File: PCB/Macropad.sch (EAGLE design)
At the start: 74 parts, among them IC1 LM2937, U1 EC11E09244AQ, X1 ZX62D-B-5PA8

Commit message: Added Matthew's urgent updates
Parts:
- added C13: 0.1uf, EE445L:CAPACITOR025-024X044
- added JP1: (no value), EE445L:PINHD-1X4
- added U2: TPD2E001DRLR, TPD2E001DRLR:TPD2E001DRLR
- C1: value 0.01uf -> 10uF
- C2, C4: value 0.1uf -> 0.1uF
- C3, C5: value 0.01uf -> 0.1uF
- C9: value 0.1uf -> 1.0uf
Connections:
- net +5V: now also C13.1, JP1.1, U2.VCC
- net D+: now also JP1.2, U2.IO1
- net D-: now also JP1.3, U2.IO2
- net GND: now also C13.2, JP1.4, U2.GND
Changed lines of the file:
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@@
 </classes>
 <parts>
-<part name="C1" library="EE445L" deviceset="CAPACITOR" device="025-024X044" value="0.01uf"/>
-<part name="C2" library="EE445L" deviceset="CAPACITOR" device="025-024X044" value="0.1uf"/>
-<part name="C3" library="EE445L" deviceset="CAPACITOR" device="025-024X044" value="0.01uf"/>
-<part name="C4" library="EE445L" deviceset="CAPACITOR" device="025-024X044" value="0.1uf"/>
-<part name="C5" library="EE445L" deviceset="CAPACITOR" device="025-024X044" value="0.01uf"/>
+<part name="C1" library="EE445L" deviceset="CAPACITOR" device="025-024X044" value="10uF"/>
+<part name="C2" library="EE445L" deviceset="CAPACITOR" device="025-024X044" value="0.1uF"/>
+<part name="C3" library="EE445L" deviceset="CAPACITOR" device="025-024X044" value="0.1uF"/>
+<part name="C4" library="EE445L" deviceset="CAPACITOR" device="025-024X044" value="0.1uF"/>
+<part name="C5" library="EE445L" deviceset="CAPACITOR" device="025-024X044" value="0.1uF"/>
 <part name="U$1" library="EE445L" deviceset="TM4C123GH6PM" device=""/>
 <part name="+3V1" library="EE445L" deviceset="+3V3" device=""/>
@@
 <part name="C7" library="EE445L" deviceset="CAPACITOR" device="025-024X044" value="0.1uf"/>
 <part name="C8" library="EE445L" deviceset="CAPACITOR" device="025-024X044" value="0.1uf"/>
-<part name="C9" library="EE445L" deviceset="CAPACITOR" device="025-024X044" value="0.1uf"/>
+<part name="C9" library="EE445L" deviceset="CAPACITOR" device="025-024X044" value="1.0uf"/>
 <part name="C10" library="EE445L" deviceset="CAPACITOR" device="025-024X044" value="2.2uf"/>
 <part name="SUPPLY3" library="EE445L" deviceset="GND" device=""/>
@@
 <part name="P+1" library="EE445L" deviceset="+5V" device=""/>
 <part name="SUPPLY6" library="EE445L" deviceset="GND" device=""/>
+<part name="U2" library="TPD2E001DRLR" deviceset="TPD2E001DRLR" device=""/>
+<part name="C13" library="EE445L" deviceset="CAPACITOR" device="025-024X044" value="0.1uf"/>
+<part name="SUPPLY10" library="EE445L" deviceset="GND" device=""/>
+<part name="P+3" library="EE445L" deviceset="+5V" device=""/>
+<part name="P+4" library="EE445L" deviceset="+5V" device=""/>
+<part name="SUPPLY12" library="EE445L" deviceset="GND" device=""/>
+<part name="JP1" library="EE445L" deviceset="PINHD-1X4" device=""/>
 </parts>
 <sheets>
@@
 <instance part="SUPPLY6" gate="GND" x="457.2" y="68.58" smashed="yes" rot="R270">
 <attribute name="VALUE" x="452.501" y="73.025" size="1.778" layer="96" rot="R270"/>
+</instance>
+<instance part="U2" gate="G$1" x="523.24" y="73.66" smashed="yes">
+<attribute name="NAME" x="510.54" y="84.82" size="2.0828" layer="95" ratio="10" rot="SR0"/>
+<attribute name="VALUE" x="510.54" y="59.5" size="2.0828" layer="96" ratio="10" rot="SR0"/>
+</instance>
+<instance part="C13" gate="G$1" x="544.83" y="77.47" smashed="yes">
+<attribute name="NAME" x="545.846" y="78.105" size="1.778" layer="95"/>
+<attribute name="VALUE" x="545.846" y="73.279" size="1.778" layer="96"/>
+</instance>
+<instance part="SUPPLY10" gate="GND" x="543.56" y="66.04" smashed="yes">
+<attribute name="VALUE" x="539.115" y="61.341" size="1.778" layer="96"/>
+</instance>
+<instance part="P+3" gate="1" x="543.56" y="83.82" smashed="yes">
+<attribute name="VALUE" x="541.02" y="78.74" size="1.778" layer="96" rot="R90"/>
+</instance>
+<instance part="P+4" gate="1" x="467.36" y="119.38" smashed="yes">
+<attribute name="VALUE" x="464.82" y="114.3" size="1.778" layer="96" rot="R90"/>
+</instance>
+<instance part="SUPPLY12" gate="GND" x="467.36" y="91.44" smashed="yes">
+<attribute name="VALUE" x="462.915" y="86.741" size="1.778" layer="96"/>
+</instance>
+<instance part="JP1" gate="A" x="480.06" y="104.14" smashed="yes">
+<attribute name="NAME" x="473.71" y="112.395" size="1.778" layer="95"/>
+<attribute name="VALUE" x="473.71" y="96.52" size="1.778" layer="96"/>
 </instance>
 </instances>
@@
 <wire x1="469.9" y1="68.58" x2="459.74" y2="68.58" width="0.1524" layer="91"/>
 <pinref part="SUPPLY6" gate="GND" pin="GND"/>
+</segment>
+<segment>
+<pinref part="C13" gate="G$1" pin="2"/>
+<pinref part="U2" gate="G$1" pin="GND"/>
+<wire x1="544.83" y1="72.39" x2="544.83" y2="68.58" width="0.1524" layer="91"/>
+<wire x1="544.83" y1="68.58" x2="543.56" y2="68.58" width="0.1524" layer="91"/>
+<pinref part="SUPPLY10" gate="GND" pin="GND"/>
+<wire x1="543.56" y1="68.58" x2="541.02" y2="68.58" width="0.1524" layer="91"/>
+<junction x="543.56" y="68.58"/>
+</segment>
+<segment>
+<wire x1="477.52" y1="101.6" x2="467.36" y2="101.6" width="0.1524" layer="91"/>
+<wire x1="467.36" y1="101.6" x2="467.36" y2="93.98" width="0.1524" layer="91"/>
+<pinref part="SUPPLY12" gate="GND" pin="GND"/>
+<pinref part="JP1" gate="A" pin="4"/>
 </segment>
 </net>
@@
 <pinref part="P+1" gate="1" pin="+5V"/>
 </segment>
+<segment>
+<pinref part="C13" gate="G$1" pin="1"/>
+<pinref part="U2" gate="G$1" pin="VCC"/>
+<wire x1="544.83" y1="80.01" x2="544.83" y2="81.28" width="0.1524" layer="91"/>
+<wire x1="544.83" y1="81.28" x2="543.56" y2="81.28" width="0.1524" layer="91"/>
+<pinref part="P+3" gate="1" pin="+5V"/>
+<wire x1="543.56" y1="81.28" x2="541.02" y2="81.28" width="0.1524" layer="91"/>
+<junction x="543.56" y="81.28"/>
+</segment>
+<segment>
+<wire x1="477.52" y1="109.22" x2="467.36" y2="109.22" width="0.1524" layer="91"/>
+<wire x1="467.36" y1="109.22" x2="467.36" y2="116.84" width="0.1524" layer="91"/>
+<pinref part="P+4" gate="1" pin="+5V"/>
+<pinref part="JP1" gate="A" pin="1"/>
+</segment>
 </net>
 <net name="RESET" class="0">
@@
 <label x="462.28" y="73.66" size="1.778" layer="95"/>
 </segment>
+<segment>
+<pinref part="U2" gate="G$1" pin="IO1"/>
+<wire x1="505.46" y1="76.2" x2="500.38" y2="76.2" width="0.1524" layer="91"/>
+<label x="500.38" y="76.2" size="1.778" layer="95"/>
+</segment>
+<segment>
+<wire x1="477.52" y1="106.68" x2="467.36" y2="106.68" width="0.1524" layer="91"/>
+<label x="464.82" y="106.68" size="1.778" layer="95"/>
+<pinref part="JP1" gate="A" pin="2"/>
+</segment>
 </net>
 <net name="D-" class="0">
@@
 <label x="462.28" y="76.2" size="1.778" layer="95"/>
 </segment>
-</net>
+<segment>
+<pinref part="U2" gate="G$1" pin="IO2"/>
+<wire x1="505.46" y1="73.66" x2="500.38" y2="73.66" width="0.1524" layer="91"/>
+<label x="500.38" y="73.66" size="1.778" layer="95"/>
+</segment>
+<segment>
+<wire x1="477.52" y1="104.14" x2="467.36" y2="104.14" width="0.1524" layer="91"/>
+<label x="464.82" y="104.14" size="1.778" layer="95"/>
+<pinref part="JP1" gate="A" pin="3"/>
+</segment>
+</net>

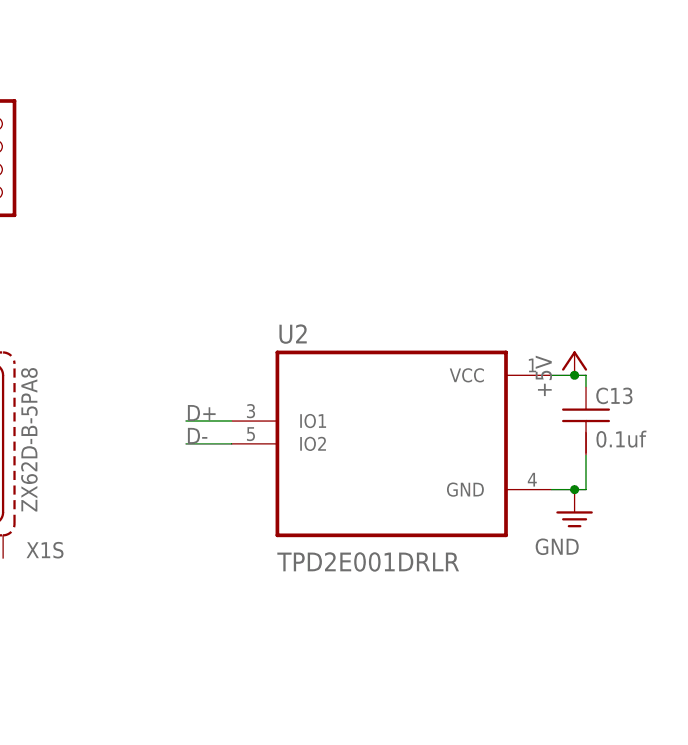
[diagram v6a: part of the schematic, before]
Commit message: Changed TVS part
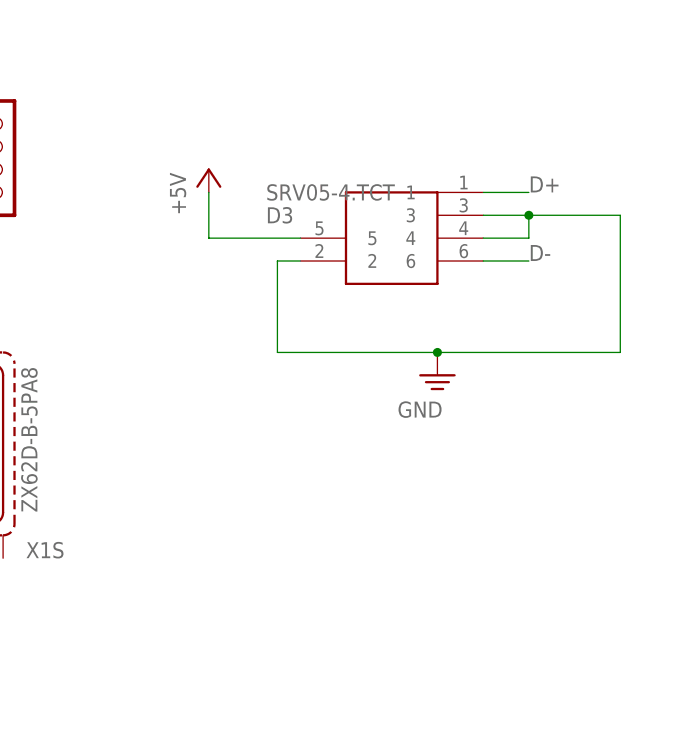
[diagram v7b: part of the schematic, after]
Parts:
- removed C13: 0.1uf, EE445L:CAPACITOR025-024X044
- removed U2: TPD2E001DRLR, TPD2E001DRLR:TPD2E001DRLR
- added D3: SRV05-4.TCT, SRV05-4.TCT:SRV05-4.TCT
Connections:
- net +5V: now also D3.5; no longer C13.1, U2.VCC
- net D+: now also D3.1; no longer U2.IO1
- net D-: now also D3.6; no longer U2.IO2
- net GND: now also D3.2, D3.3, D3.4; no longer C13.2, U2.GND
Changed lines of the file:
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@@
 <part name="P+1" library="EE445L" deviceset="+5V" device=""/>
 <part name="SUPPLY6" library="EE445L" deviceset="GND" device=""/>
-<part name="U2" library="TPD2E001DRLR" deviceset="TPD2E001DRLR" device=""/>
-<part name="C13" library="EE445L" deviceset="CAPACITOR" device="025-024X044" value="0.1uf"/>
 <part name="SUPPLY10" library="EE445L" deviceset="GND" device=""/>
 <part name="P+3" library="EE445L" deviceset="+5V" device=""/>
@@
 <part name="SUPPLY12" library="EE445L" deviceset="GND" device=""/>
 <part name="JP1" library="EE445L" deviceset="PINHD-1X4" device=""/>
+<part name="D3" library="SRV05-4.TCT" deviceset="SRV05-4.TCT" device=""/>
 </parts>
 <sheets>
@@
 <attribute name="VALUE" x="452.501" y="73.025" size="1.778" layer="96" rot="R270"/>
 </instance>
-<instance part="U2" gate="G$1" x="523.24" y="73.66" smashed="yes">
-<attribute name="NAME" x="510.54" y="84.82" size="2.0828" layer="95" ratio="10" rot="SR0"/>
-<attribute name="VALUE" x="510.54" y="59.5" size="2.0828" layer="96" ratio="10" rot="SR0"/>
-</instance>
-<instance part="C13" gate="G$1" x="544.83" y="77.47" smashed="yes">
-<attribute name="NAME" x="545.846" y="78.105" size="1.778" layer="95"/>
-<attribute name="VALUE" x="545.846" y="73.279" size="1.778" layer="96"/>
-</instance>
-<instance part="SUPPLY10" gate="GND" x="543.56" y="66.04" smashed="yes">
-<attribute name="VALUE" x="539.115" y="61.341" size="1.778" layer="96"/>
-</instance>
-<instance part="P+3" gate="1" x="543.56" y="83.82" smashed="yes">
-<attribute name="VALUE" x="541.02" y="78.74" size="1.778" layer="96" rot="R90"/>
+<instance part="SUPPLY10" gate="GND" x="528.32" y="81.28" smashed="yes">
+<attribute name="VALUE" x="523.875" y="76.581" size="1.778" layer="96"/>
+</instance>
+<instance part="P+3" gate="1" x="502.92" y="104.14" smashed="yes">
+<attribute name="VALUE" x="500.38" y="99.06" size="1.778" layer="96" rot="R90"/>
 </instance>
 <instance part="P+4" gate="1" x="467.36" y="119.38" smashed="yes">
@@
 <attribute name="NAME" x="473.71" y="112.395" size="1.778" layer="95"/>
 <attribute name="VALUE" x="473.71" y="96.52" size="1.778" layer="96"/>
+</instance>
+<instance part="D3" gate="G$1" x="513.08" y="99.06" smashed="yes">
+<attribute name="NAME" x="509.27" y="99.06" size="1.778" layer="95" align="center-left"/>
+<attribute name="VALUE" x="509.27" y="101.6" size="1.778" layer="96" align="center-left"/>
 </instance>
 </instances>
@@
 </segment>
 <segment>
-<pinref part="C13" gate="G$1" pin="2"/>
-<pinref part="U2" gate="G$1" pin="GND"/>
-<wire x1="544.83" y1="72.39" x2="544.83" y2="68.58" width="0.1524" layer="91"/>
-<wire x1="544.83" y1="68.58" x2="543.56" y2="68.58" width="0.1524" layer="91"/>
-<pinref part="SUPPLY10" gate="GND" pin="GND"/>
-<wire x1="543.56" y1="68.58" x2="541.02" y2="68.58" width="0.1524" layer="91"/>
-<junction x="543.56" y="68.58"/>
-</segment>
-<segment>
 <wire x1="477.52" y1="101.6" x2="467.36" y2="101.6" width="0.1524" layer="91"/>
 <wire x1="467.36" y1="101.6" x2="467.36" y2="93.98" width="0.1524" layer="91"/>
 <pinref part="SUPPLY12" gate="GND" pin="GND"/>
 <pinref part="JP1" gate="A" pin="4"/>
+</segment>
+<segment>
+<pinref part="D3" gate="G$1" pin="2"/>
+<wire x1="513.08" y1="93.98" x2="510.54" y2="93.98" width="0.1524" layer="91"/>
+<wire x1="510.54" y1="93.98" x2="510.54" y2="83.82" width="0.1524" layer="91"/>
+<pinref part="D3" gate="G$1" pin="3"/>
+<wire x1="533.4" y1="99.06" x2="538.48" y2="99.06" width="0.1524" layer="91"/>
+<wire x1="538.48" y1="99.06" x2="548.64" y2="99.06" width="0.1524" layer="91"/>
+<wire x1="548.64" y1="99.06" x2="548.64" y2="83.82" width="0.1524" layer="91"/>
+<wire x1="548.64" y1="83.82" x2="528.32" y2="83.82" width="0.1524" layer="91"/>
+<pinref part="SUPPLY10" gate="GND" pin="GND"/>
+<wire x1="528.32" y1="83.82" x2="510.54" y2="83.82" width="0.1524" layer="91"/>
+<junction x="528.32" y="83.82"/>
+<pinref part="D3" gate="G$1" pin="4"/>
+<wire x1="533.4" y1="96.52" x2="538.48" y2="96.52" width="0.1524" layer="91"/>
+<wire x1="538.48" y1="96.52" x2="538.48" y2="99.06" width="0.1524" layer="91"/>
+<junction x="538.48" y="99.06"/>
 </segment>
 </net>
@@
 </segment>
 <segment>
-<pinref part="C13" gate="G$1" pin="1"/>
-<pinref part="U2" gate="G$1" pin="VCC"/>
-<wire x1="544.83" y1="80.01" x2="544.83" y2="81.28" width="0.1524" layer="91"/>
-<wire x1="544.83" y1="81.28" x2="543.56" y2="81.28" width="0.1524" layer="91"/>
-<pinref part="P+3" gate="1" pin="+5V"/>
-<wire x1="543.56" y1="81.28" x2="541.02" y2="81.28" width="0.1524" layer="91"/>
-<junction x="543.56" y="81.28"/>
-</segment>
-<segment>
 <wire x1="477.52" y1="109.22" x2="467.36" y2="109.22" width="0.1524" layer="91"/>
 <wire x1="467.36" y1="109.22" x2="467.36" y2="116.84" width="0.1524" layer="91"/>
 <pinref part="P+4" gate="1" pin="+5V"/>
 <pinref part="JP1" gate="A" pin="1"/>
+</segment>
+<segment>
+<pinref part="D3" gate="G$1" pin="5"/>
+<wire x1="513.08" y1="96.52" x2="502.92" y2="96.52" width="0.1524" layer="91"/>
+<wire x1="502.92" y1="96.52" x2="502.92" y2="101.6" width="0.1524" layer="91"/>
+<pinref part="P+3" gate="1" pin="+5V"/>
 </segment>
 </net>
@@
 </segment>
 <segment>
-<pinref part="U2" gate="G$1" pin="IO1"/>
-<wire x1="505.46" y1="76.2" x2="500.38" y2="76.2" width="0.1524" layer="91"/>
-<label x="500.38" y="76.2" size="1.778" layer="95"/>
+<wire x1="538.48" y1="101.6" x2="533.4" y2="101.6" width="0.1524" layer="91"/>
+<label x="538.48" y="101.6" size="1.778" layer="95"/>
+<pinref part="D3" gate="G$1" pin="1"/>
 </segment>
 <segment>
@@
 </segment>
 <segment>
-<pinref part="U2" gate="G$1" pin="IO2"/>
-<wire x1="505.46" y1="73.66" x2="500.38" y2="73.66" width="0.1524" layer="91"/>
-<label x="500.38" y="73.66" size="1.778" layer="95"/>
-</segment>
-<segment>
 <wire x1="477.52" y1="104.14" x2="467.36" y2="104.14" width="0.1524" layer="91"/>
 <label x="464.82" y="104.14" size="1.778" layer="95"/>
 <pinref part="JP1" gate="A" pin="3"/>
 </segment>
-</net>
+<segment>
+<pinref part="D3" gate="G$1" pin="6"/>
+<wire x1="533.4" y1="93.98" x2="538.48" y2="93.98" width="0.1524" layer="91"/>
+<label x="538.48" y="93.98" size="1.778" layer="95"/>
+</segment>
+</net>

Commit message: Added not urgent but recommended updates
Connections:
- net GND: now also X1G$1.4
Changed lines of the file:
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@@
 <attribute name="VALUE" x="79.375" y="145.161" size="1.778" layer="96"/>
 </instance>
-<instance part="FRAME3" gate="G$1" x="289.56" y="226.06" smashed="yes"/>
 <instance part="FRAME3" gate="G$2" x="462.28" y="228.6" smashed="yes">
 <attribute name="LAST_DATE_TIME" x="474.98" y="229.87" size="2.54" layer="94"/>
@@
 <attribute name="NAME" x="482.6" y="60.96" size="1.778" layer="95" font="vector"/>
 </instance>
-<instance part="P+1" gate="1" x="457.2" y="78.74" smashed="yes" rot="R90">
-<attribute name="VALUE" x="457.2" y="78.74" size="1.778" layer="96" rot="R180"/>
-</instance>
-<instance part="SUPPLY6" gate="GND" x="457.2" y="68.58" smashed="yes" rot="R270">
-<attribute name="VALUE" x="452.501" y="73.025" size="1.778" layer="96" rot="R270"/>
+<instance part="P+1" gate="1" x="457.2" y="81.28" smashed="yes">
+<attribute name="VALUE" x="457.2" y="83.82" size="1.778" layer="96" rot="R180"/>
+</instance>
+<instance part="SUPPLY6" gate="GND" x="457.2" y="66.04" smashed="yes">
+<attribute name="VALUE" x="452.755" y="61.341" size="1.778" layer="96"/>
 </instance>
 <instance part="SUPPLY10" gate="GND" x="528.32" y="81.28" smashed="yes">
@@
 <segment>
 <pinref part="X1" gate="G$1" pin="5"/>
-<wire x1="469.9" y1="68.58" x2="459.74" y2="68.58" width="0.1524" layer="91"/>
+<wire x1="469.9" y1="68.58" x2="464.82" y2="68.58" width="0.1524" layer="91"/>
 <pinref part="SUPPLY6" gate="GND" pin="GND"/>
+<pinref part="X1" gate="G$1" pin="4"/>
+<wire x1="464.82" y1="68.58" x2="457.2" y2="68.58" width="0.1524" layer="91"/>
+<wire x1="469.9" y1="71.12" x2="464.82" y2="71.12" width="0.1524" layer="91"/>
+<wire x1="464.82" y1="71.12" x2="464.82" y2="68.58" width="0.1524" layer="91"/>
+<junction x="464.82" y="68.58"/>
 </segment>
 <segment>
@@
 <segment>
 <pinref part="X1" gate="G$1" pin="1"/>
-<wire x1="469.9" y1="78.74" x2="459.74" y2="78.74" width="0.1524" layer="91"/>
+<wire x1="469.9" y1="78.74" x2="457.2" y2="78.74" width="0.1524" layer="91"/>
 <pinref part="P+1" gate="1" pin="+5V"/>
 </segment>
